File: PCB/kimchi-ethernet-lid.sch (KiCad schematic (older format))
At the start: 8 parts, among them J1 DF40HC(3.5)-60DS, J2 DF40HC(3.5)-60DS, U1 24C32

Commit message: Libraries, Schematic Capture, Part Placement, Lauout
Created and added all realted components. Completed schematic capture. Part placement all bu down, layout in progress since schematic capture.

Had to change out mag jacks a lot to find one that would fit the design
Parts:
- removed H1, H2, H3, H4: MountingHole_Pad, kimchi_ulid:MountingHole_3mm_Pad, symbol Mechanical:MountingHole_Pad
- removed LOGO1: Logo_Open_Hardware_Small, Symbol:OSHW-Logo_5.7x6mm_SilkScreen, symbol Graphic:Logo_Open_Hardware_Small
- added C1, C10, C11, C12, C13, C14, C19, C2, C20, C3, C4, C5, C6, C7, C8: C0402C104K9PACTU, AVR-KiCAD-Lib-Resistors:R0402, symbol kimchi_ulid:C0402C104K9PACTU
- added C15, C9: 0402ZD105KAT2A, AVR-KiCAD-Lib-Resistors:R0402, symbol kimchi_ulid:0402ZD105KAT2A
- added C16: GRM155R61A475MEAAD, kimchi_ulid:C0402, symbol kimchi_ulid:GRM155R61A475MEAAD
- added C17, C18: 04025A180GAT2A, kimchi_ulid:C0402, symbol kimchi_ulid:04025A180GAT2A
- added C21: C0603C103KARACAUTO, kimchi_ulid:C0603, symbol kimchi_ulid:C0603C103KARACAUTO
- added FB1, FB2, FB3: MMZ1005S601CTD25, kimchi_ulid:R0402, symbol kimchi_ulid:MMZ1005S601CTD25
- added H1, H2, H3, H4: Mechanical_MountingHole_Pad, kimchi_ulid:MountingHole_3mm_Pad, symbol kimchi_ulid:Mechanical_MountingHole_Pad
- added J3: ARJM11C7-502-AB-ER2-T, ABRACON_ARJM11C7-502-AB-ER2-T, symbol kimchi_ulid:ARJM11C7-502-AB-ER2-T
- added L1: GG_LOGO, symbol kimchi_ulid:GG_LOGO
- added LOGO1: Graphic_Logo_Open_Hardware_Small, kimchi_ulid:OSHW-Logo_5.7x6mm_SilkScreen, symbol kimchi_ulid:Graphic_Logo_Open_Hardware_Small
- added R1, R15, R16, R20, R?: RC0402FR-071KL, kimchi_ulid:R0402, symbol kimchi_ulid:RC0402FR-071KL
- added R10, R11, R12, R21, R22, R23, R24, R25, R26, R7, R8, R9: RC0402FR-0722RL, kimchi_ulid:R0402, symbol kimchi_ulid:RC0402FR-0722RL
- added R13: RC0402FR-074K7L, kimchi_ulid:R0402, symbol kimchi_ulid:RC0402FR-074K7L
- added R17: RC0402FR-0710KL, kimchi_ulid:R0402, symbol kimchi_ulid:RC0402FR-0710KL
- added R18: RMCF0402FT12K1, kimchi_ulid:R0402, symbol kimchi_ulid:RMCF0402FT12K1
- added U3: KSZ9031RNXCC, kimchi_ulid:QFN50P700X700X90-49N, symbol kimchi_ulid:KSZ9031RNXCC
- added U4: TLV73312PDQNR3, kimchi_ulid:TLV73312PDQNR3, symbol kimchi_ulid:TLV73312PDQNR3
- added Y1: ABM3-25.000MHZ-D2Y-T, XTAL500X320X130N, symbol kimchi_ulid:ABM3-25.000MHZ-D2Y-T
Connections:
- net labels added: LED1, LED2, SYS_RESET, TRD1+, TRD1-, TRD2+, TRD2-, TRD3+, TRD3-, TRD4+, TRD4-, VDD_PHY_1V2, XI, XO
- wire segments 59 -> 225

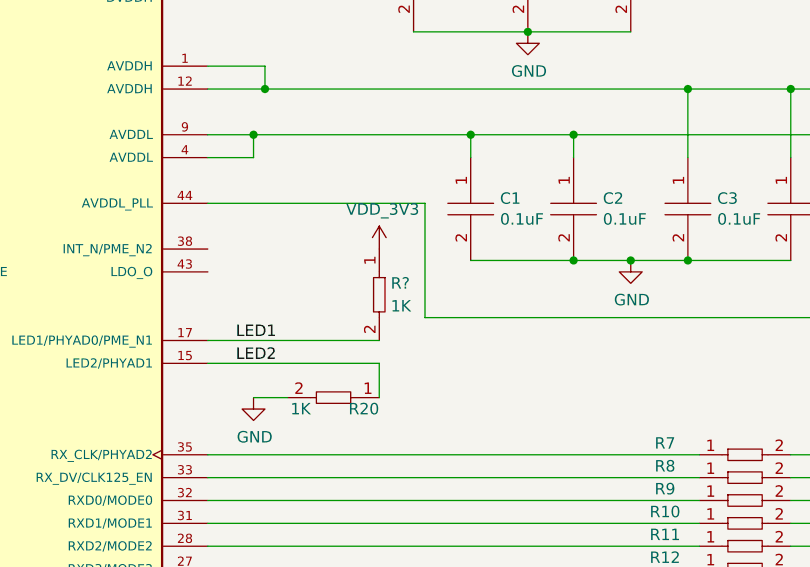
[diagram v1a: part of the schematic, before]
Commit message: small schematic tweak that didn't get synced
d
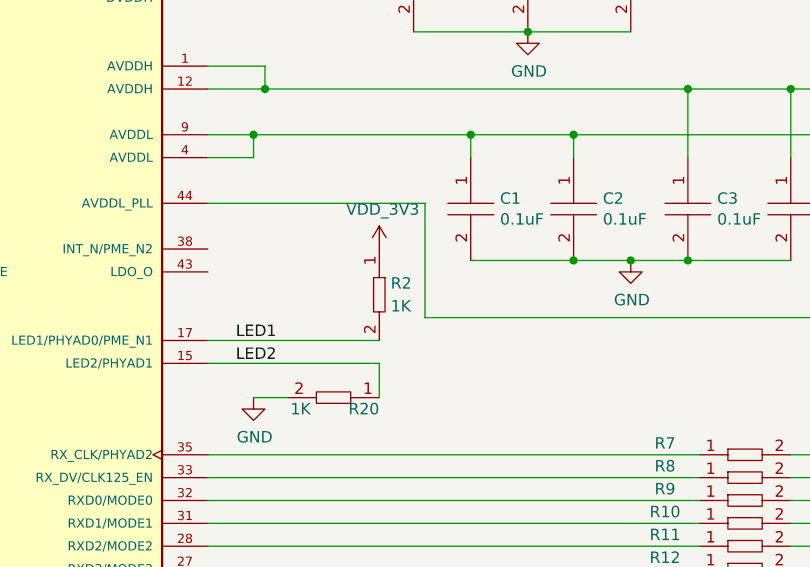
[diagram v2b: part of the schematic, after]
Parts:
- gave numbers to parts that had none: 1
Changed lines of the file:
@@
 $EndComp
 $Comp
-L kimchi_ulid:RC0402FR-071KL R?
+L kimchi_ulid:RC0402FR-071KL R2
 U 1 1 6154EE9A
 P 9800 7750
-F 0 "R?" V 9750 7800 50  0000 L CNN
+F 0 "R2" V 9750 7800 50  0000 L CNN
 F 1 "RC0402FR-071KL" H 9800 7975 50  0001 C CNN
 F 2 "kimchi_ulid:R0402" H 9800 7750 50  0001 C CNN
@@
 $EndComp
 $Comp
-L kimchi_ulid:VDD_3V3 #PWR?
+L kimchi_ulid:VDD_3V3 #PWR0133
 U 1 1 6155AF6B
 P 9800 7550
-F 0 "#PWR?" H 9800 7400 50  0001 C CNN
+F 0 "#PWR0133" H 9800 7400 50  0001 C CNN
 F 1 "VDD_3V3" H 9815 7723 50  0000 C CNN
 F 2 "" H 9800 7550 50  0001 C CNN

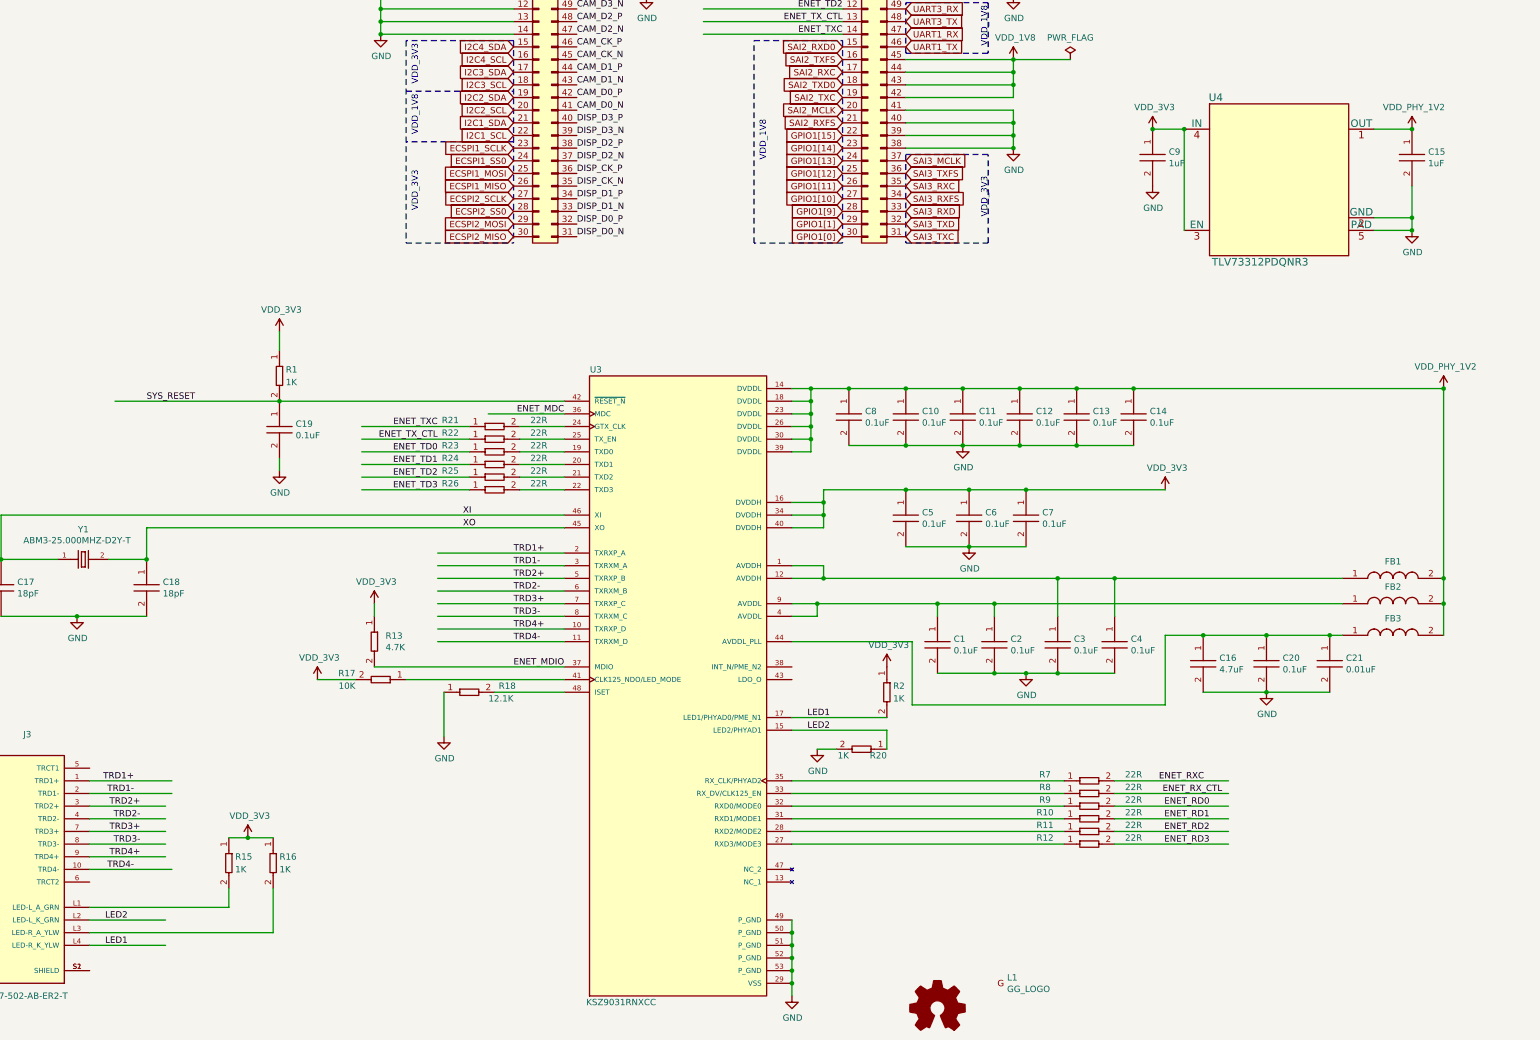
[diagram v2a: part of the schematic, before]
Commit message: Route Complete
RMGII signals routed to kimchi headers, ENET diff pairs tuned routed to connector. Power distribution scheme designed and implemented. First pass of route done, Further analysis need for RGMII interface trace length tuning
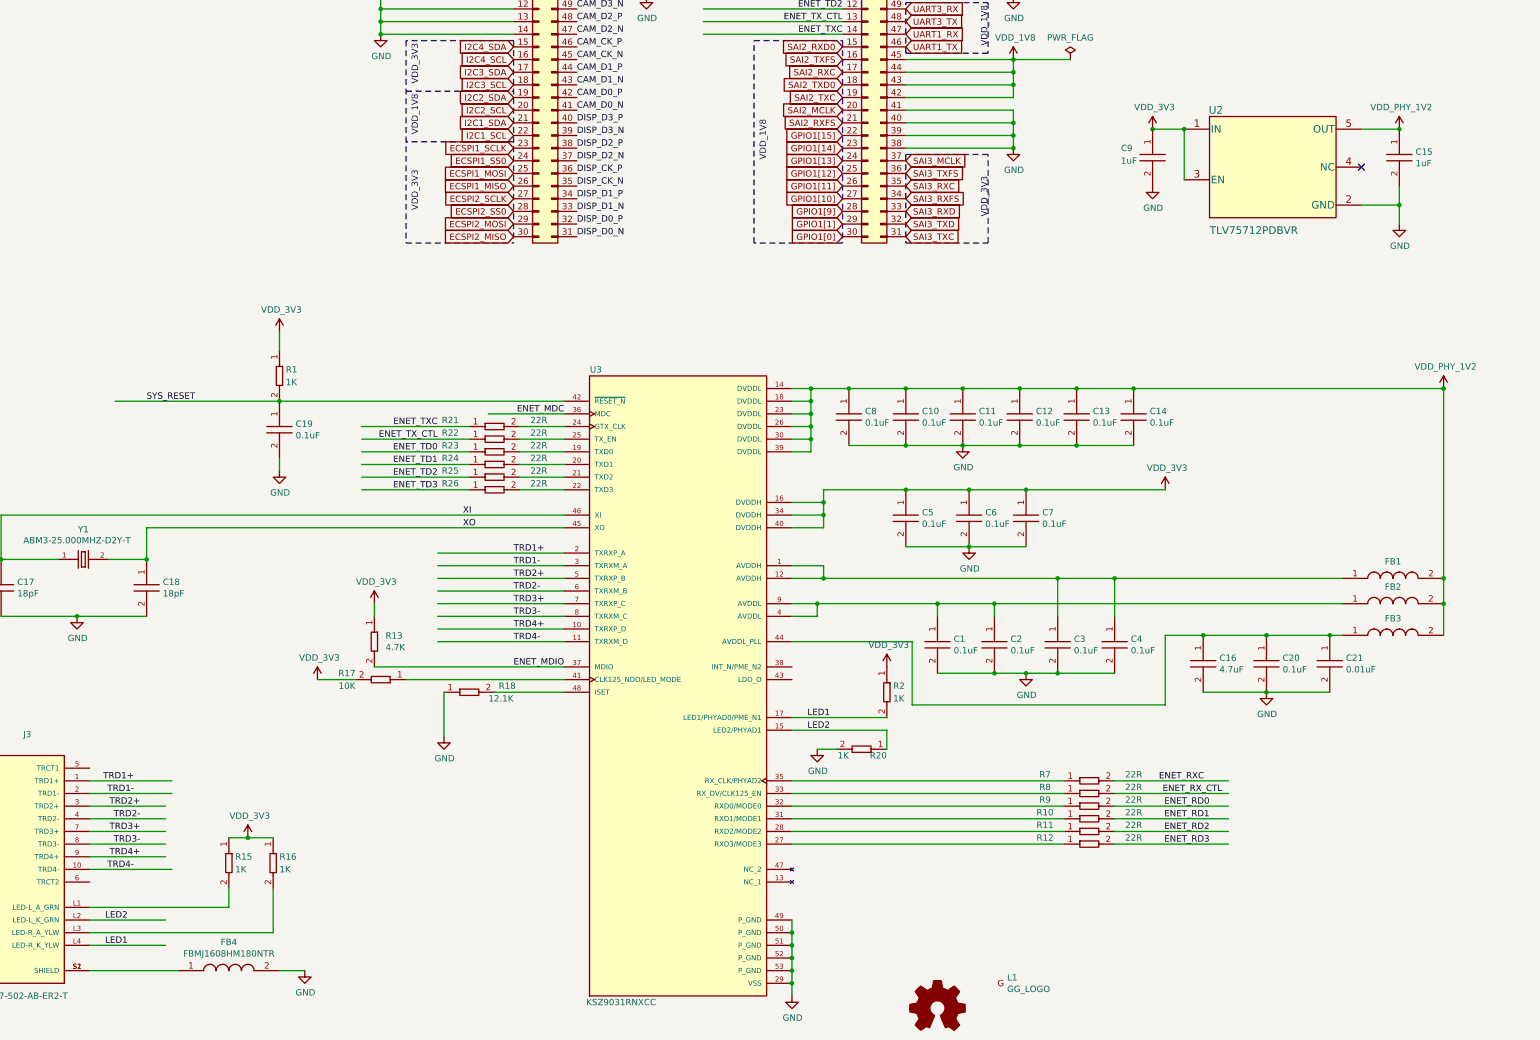
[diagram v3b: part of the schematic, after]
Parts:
- removed U4: TLV73312PDQNR3, kimchi_ulid:TLV73312PDQNR3, symbol kimchi_ulid:TLV73312PDQNR3
- added FB4: FBMJ1608HM180NTR, kimchi_ulid:R0603, symbol kimchi_ulid:FBMJ1608HM180NTR
- added U2: TLV75712PDBVR, kimchi_ulid:TLV75712PDBVR, symbol kimchi_ulid:TLV75712PDBVR
- L1: footprint (none) -> kimchi_ulid:groupgets_logo
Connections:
- wire segments 225 -> 226
- no-connect marks 0 -> 1
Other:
- moved on the sheet: C15
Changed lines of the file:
@@
-$EndComp
-$Comp
-L kimchi_ulid:TLV73312PDQNR3 U4
-U 1 1 608AF12E
-P 12850 3700
-F 0 "U4" H 12400 4350 60  0000 C CNN
-F 1 "TLV73312PDQNR3" H 12750 3050 60  0000 C CNN
-F 2 "kimchi_ulid:TLV73312PDQNR3" H 12750 2940 60  0001 C CNN
-F 3 "" H 12750 3000 60  0000 C CNN
-	1    12850 3700
-	1    0    0    -1
 $EndComp
 $Comp
@@
 U 1 1 608BADEE
 P 11900 3500
-F 0 "C9" V 11879 3628 50  0000 L CNN
+F 0 "C9" V 11850 3250 50  0000 L CNN
 F 1 "0402ZD105KAT2A" H 11950 3700 50  0001 C CNN
 F 2 "AVR-KiCAD-Lib-Resistors:R0402" H 11700 3500 50  0001 C CNN
@@
 F 25 "0402" H 14000 5800 50  0001 C CNN "Package"
 F 26 "±10% 10V Ceramic Capacitor X5R 0402 (1005 Metric)" H 14400 6200 50  0001 C CNN "Description"
-F 27 "1uF" V 11970 3628 50  0000 L CNN "_Value_"
+F 27 "1uF" V 11950 3250 50  0000 L CNN "_Value_"
 F 28 "*" H 14300 6100 50  0001 C CNN "Management_ID"
 	1    11900 3500
@@
 L kimchi_ulid:0402ZD105KAT2A C15
 U 1 1 60915F14
-P 13950 3500
-F 0 "C15" V 13929 3628 50  0000 L CNN
-F 1 "0402ZD105KAT2A" H 14000 3700 50  0001 C CNN
-F 2 "AVR-KiCAD-Lib-Resistors:R0402" H 13750 3500 50  0001 C CNN
-F 3 "https://datasheets.avx.com/cx5r.pdf" H 13850 3600 50  0001 C CNN
-F 4 "0.13000" H 14050 3750 50  0001 C CNN "Cost QTY: 1"
-F 5 "0.02610" H 14150 3850 50  0001 C CNN "Cost QTY: 1000"
-F 6 "0.02430" H 14250 3950 50  0001 C CNN "Cost QTY: 2500"
-F 7 "0.02223" H 14350 4050 50  0001 C CNN "Cost QTY: 5000"
-F 8 "0.02068" H 14450 4150 50  0001 C CNN "Cost QTY: 10000"
-F 9 "AVX Corporation" H 14550 4250 50  0001 C CNN "MFR"
-F 10 "0402ZD105KAT2A" H 14650 4350 50  0001 C CNN "MFR#"
-F 11 "Digikey" H 14750 4450 50  0001 C CNN "Vendor"
-F 12 "478-4596-1-ND" H 14850 4550 50  0001 C CNN "Vendor #"
-F 13 "AVR" H 14950 4650 50  0001 C CNN "Designer"
-F 14 "0.55mm" H 15050 4750 50  0001 C CNN "Height"
-F 15 "4/27/2021" H 16150 5850 50  0001 C CNN "Date Created"
-F 16 "4/27/2021" H 15150 4850 50  0001 C CNN "Date Modified"
-F 17 "Yes" H 15250 4950 50  0001 C CNN "Lead-Free ?"
-F 18 "1" H 15350 5050 50  0001 C CNN "RoHS Levels"
-F 19 "SMT" H 15450 5150 50  0001 C CNN "Mounting"
-F 20 "2" H 15550 5250 50  0001 C CNN "Pin Count #"
-F 21 "Active" H 15650 5350 50  0001 C CNN "Status"
-F 22 "10%" H 15750 5450 50  0001 C CNN "Tolerance"
-F 23 "Ceramic Cap" H 15850 5550 50  0001 C CNN "Type"
-F 24 "10V" H 15950 5650 50  0001 C CNN "Voltage"
-F 25 "0402" H 16050 5800 50  0001 C CNN "Package"
-F 26 "±10% 10V Ceramic Capacitor X5R 0402 (1005 Metric)" H 16450 6200 50  0001 C CNN "Description"
-F 27 "1uF" V 14020 3628 50  0000 L CNN "_Value_"
-F 28 "*" H 16350 6100 50  0001 C CNN "Management_ID"
-	1    13950 3500
-	0    1    1    0
-$EndComp
-Wire Wire Line
-	13950 3300 13650 3300
-Wire Wire Line
-	13650 4100 13950 4100
-Wire Wire Line
-	13950 4100 13950 4000
-Wire Wire Line
-	13650 4000 13950 4000
-Connection ~ 13950 4000
-Wire Wire Line
-	13950 4000 13950 3750
+P 13850 3500
+F 0 "C15" V 13829 3628 50  0000 L CNN
+F 1 "0402ZD105KAT2A" H 13900 3700 50  0001 C CNN
+F 2 "AVR-KiCAD-Lib-Resistors:R0402" H 13650 3500 50  0001 C CNN
+F 3 "https://datasheets.avx.com/cx5r.pdf" H 13750 3600 50  0001 C CNN
+F 4 "0.13000" H 13950 3750 50  0001 C CNN "Cost QTY: 1"
+F 5 "0.02610" H 14050 3850 50  0001 C CNN "Cost QTY: 1000"
+F 6 "0.02430" H 14150 3950 50  0001 C CNN "Cost QTY: 2500"
+F 7 "0.02223" H 14250 4050 50  0001 C CNN "Cost QTY: 5000"
+F 8 "0.02068" H 14350 4150 50  0001 C CNN "Cost QTY: 10000"
+F 9 "AVX Corporation" H 14450 4250 50  0001 C CNN "MFR"
+F 10 "0402ZD105KAT2A" H 14550 4350 50  0001 C CNN "MFR#"
+F 11 "Digikey" H 14650 4450 50  0001 C CNN "Vendor"
+F 12 "478-4596-1-ND" H 14750 4550 50  0001 C CNN "Vendor #"
+F 13 "AVR" H 14850 4650 50  0001 C CNN "Designer"
+F 14 "0.55mm" H 14950 4750 50  0001 C CNN "Height"
+F 15 "4/27/2021" H 16050 5850 50  0001 C CNN "Date Created"
+F 16 "4/27/2021" H 15050 4850 50  0001 C CNN "Date Modified"
+F 17 "Yes" H 15150 4950 50  0001 C CNN "Lead-Free ?"
+F 18 "1" H 15250 5050 50  0001 C CNN "RoHS Levels"
+F 19 "SMT" H 15350 5150 50  0001 C CNN "Mounting"
+F 20 "2" H 15450 5250 50  0001 C CNN "Pin Count #"
+F 21 "Active" H 15550 5350 50  0001 C CNN "Status"
+F 22 "10%" H 15650 5450 50  0001 C CNN "Tolerance"
+F 23 "Ceramic Cap" H 15750 5550 50  0001 C CNN "Type"
+F 24 "10V" H 15850 5650 50  0001 C CNN "Voltage"
+F 25 "0402" H 15950 5800 50  0001 C CNN "Package"
+F 26 "±10% 10V Ceramic Capacitor X5R 0402 (1005 Metric)" H 16350 6200 50  0001 C CNN "Description"
+F 27 "1uF" V 13920 3628 50  0000 L CNN "_Value_"
+F 28 "*" H 16250 6100 50  0001 C CNN "Management_ID"
+	1    13850 3500
+	0    1    1    0
+$EndComp
+Wire Wire Line
+	13850 3300 13550 3300
+Wire Wire Line
+	13850 4050 13850 3900
+Wire Wire Line
+	13550 3900 13850 3900
+Connection ~ 13850 3900
+Wire Wire Line
+	13850 3900 13850 3750
 Wire Wire Line
 	11900 3300 12150 3300
-Wire Wire Line
-	12150 3300 12150 4100
-Connection ~ 12150 3300
 $Comp
 L power:GND #PWR0115
@@
 L kimchi_ulid:VDD_PHY_1V2 #PWR0119
 U 1 1 60933B5F
-P 13950 3300
-F 0 "#PWR0119" H 13950 3150 50  0001 C CNN
-F 1 "VDD_PHY_1V2" H 13965 3473 50  0000 C CNN
-F 2 "" H 13950 3300 50  0001 C CNN
-F 3 "" H 13950 3300 50  0001 C CNN
-	1    13950 3300
-	1    0    0    -1
-$EndComp
-Connection ~ 13950 3300
+P 13850 3300
+F 0 "#PWR0119" H 13850 3150 50  0001 C CNN
+F 1 "VDD_PHY_1V2" H 13865 3473 50  0000 C CNN
+F 2 "" H 13850 3300 50  0001 C CNN
+F 3 "" H 13850 3300 50  0001 C CNN
+	1    13850 3300
+	1    0    0    -1
+$EndComp
+Connection ~ 13850 3300
 Wire Wire Line
 	9450 1250 8350 1250
@@
 F 0 "L1" H 10750 10095 50  0000 L CNN
 F 1 "GG_LOGO" H 10750 10004 50  0000 L CNN
-F 2 "" H 10700 10050 50  0001 C CNN
+F 2 "kimchi_ulid:groupgets_logo" H 10700 10050 50  0001 C CNN
 F 3 "" H 10700 10050 50  0001 C CNN
 	1    10700 10050
@@
 L power:GND #PWR0128
 U 1 1 61265052
-P 13950 4100
-F 0 "#PWR0128" H 13950 3850 50  0001 C CNN
-F 1 "GND" H 13955 3927 50  0000 C CNN
-F 2 "" H 13950 4100 50  0001 C CNN
-F 3 "" H 13950 4100 50  0001 C CNN
-	1    13950 4100
-	1    0    0    -1
-$EndComp
-Connection ~ 13950 4100
+P 13850 4050
+F 0 "#PWR0128" H 13850 3800 50  0001 C CNN
+F 1 "GND" H 13855 3877 50  0000 C CNN
+F 2 "" H 13850 4050 50  0001 C CNN
+F 3 "" H 13850 4050 50  0001 C CNN
+	1    13850 4050
+	1    0    0    -1
+$EndComp
 $Comp
 L kimchi_ulid:VDD_3V3 #PWR0129
@@
 	1    0    0    -1
 $EndComp
+$Comp
+L kimchi_ulid:TLV75712PDBVR U2
+U 1 1 609227FB
+P 12350 3200
+F 0 "U2" H 12400 3250 60  0000 C CNN
+F 1 "TLV75712PDBVR" H 12700 2300 60  0000 C CNN
+F 2 "kimchi_ulid:TLV75712PDBVR" H 12600 2250 60  0001 C CNN
+F 3 "" H 12850 2800 60  0000 C CNN
+	1    12350 3200
+	1    0    0    -1
+$EndComp
+Wire Wire Line
+	12150 3700 12150 3300
+Connection ~ 12150 3300
+NoConn ~ 13550 3600
+$Comp
+L kimchi_ulid:FBMJ1608HM180NTR FB4
+U 1 1 609DED6B
+P 4600 9950
+F 0 "FB4" H 4600 10175 50  0000 C CNN
+F 1 "FBMJ1608HM180NTR" H 4650 10150 50  0001 C CNN
+F 2 "kimchi_ulid:R0603" H 4600 9950 50  0001 C CNN
+F 3 "" H 4600 9950 50  0001 C CNN
+F 4 "0.11000" H 4700 10200 50  0001 C CNN "Cost QTY: 1"
+F 5 "0.03135" H 4800 10300 50  0001 C CNN "Cost QTY: 1000"
+F 6 "0.02660" H 4900 10400 50  0001 C CNN "Cost QTY: 2500"
+F 7 "0.02850" H 5000 10500 50  0001 C CNN "Cost QTY: 5000"
+F 8 "*" H 5100 10600 50  0001 C CNN "Cost QTY: 10000"
+F 9 "Taiyo Yuden" H 5200 10700 50  0001 C CNN "MFR"
+F 10 "FBMJ1608HM180NTR" H 5300 10800 50  0001 C CNN "MFR#"
+F 11 "Digikey" H 5400 10900 50  0001 C CNN "Vendor"
+F 12 "587-3251-1-ND" H 5500 11000 50  0001 C CNN "Vendor #"
+F 13 "AVR" H 5600 11100 50  0001 C CNN "Designer"
+F 14 "1mm" H 5700 11200 50  0001 C CNN "Height"
+F 15 "12/5/2019" H 6800 12300 50  0001 C CNN "Date Created"
+F 16 "12/5/2019" H 5800 11300 50  0001 C CNN "Date Modified"
+F 17 "Yes" H 5900 11400 50  0001 C CNN "Lead-Free ?"
+F 18 "1" H 6000 11500 50  0001 C CNN "RoHS Levels"
+F 19 "SMT" H 6100 11600 50  0001 C CNN "Mounting"
+F 20 "2" H 6200 11700 50  0001 C CNN "Pin Count #"
+F 21 "Active" H 6300 11800 50  0001 C CNN "Status"
+F 22 "*" H 6400 11900 50  0001 C CNN "Tolerance"
+F 23 "Ferrite Bead" H 6500 12000 50  0001 C CNN "Type"
+F 24 "*" H 6600 12100 50  0001 C CNN "Voltage"
+F 25 "0603" H 6700 12250 50  0001 C CNN "Package"
+F 26 "FBMJ1608HM180NTR" H 4600 10084 50  0000 C CNN "_Value_"
+F 27 "*" H 7000 12550 50  0001 C CNN "Management_ID"
+F 28 "18 Ohms @ 100MHz 1 Power Line Ferrite Bead 0603 (1608 Metric) 7.5A 4mOhm" H 4600 9950 50  0001 C CNN "Description"
+	1    4600 9950
+	1    0    0    -1
+$EndComp
+Wire Wire Line
+	3500 9950 4200 9950
+$Comp
+L power:GND #PWR0134
+U 1 1 609F4BC6
+P 5200 9950
+F 0 "#PWR0134" H 5200 9700 50  0001 C CNN
+F 1 "GND" H 5205 9777 50  0000 C CNN
+F 2 "" H 5200 9950 50  0001 C CNN
+F 3 "" H 5200 9950 50  0001 C CNN
+	1    5200 9950
+	1    0    0    -1
+$EndComp
+Wire Wire Line
+	5000 9950 5200 9950
 $EndSCHEMATC
